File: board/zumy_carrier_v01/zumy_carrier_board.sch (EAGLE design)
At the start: 26 parts, among them IC1 SN74AUP2G17, IC2 SN74AUP2G17, J1 ODROID_POWER, J2 BATT_POWER, SW1 500SSP1S1M6QEA

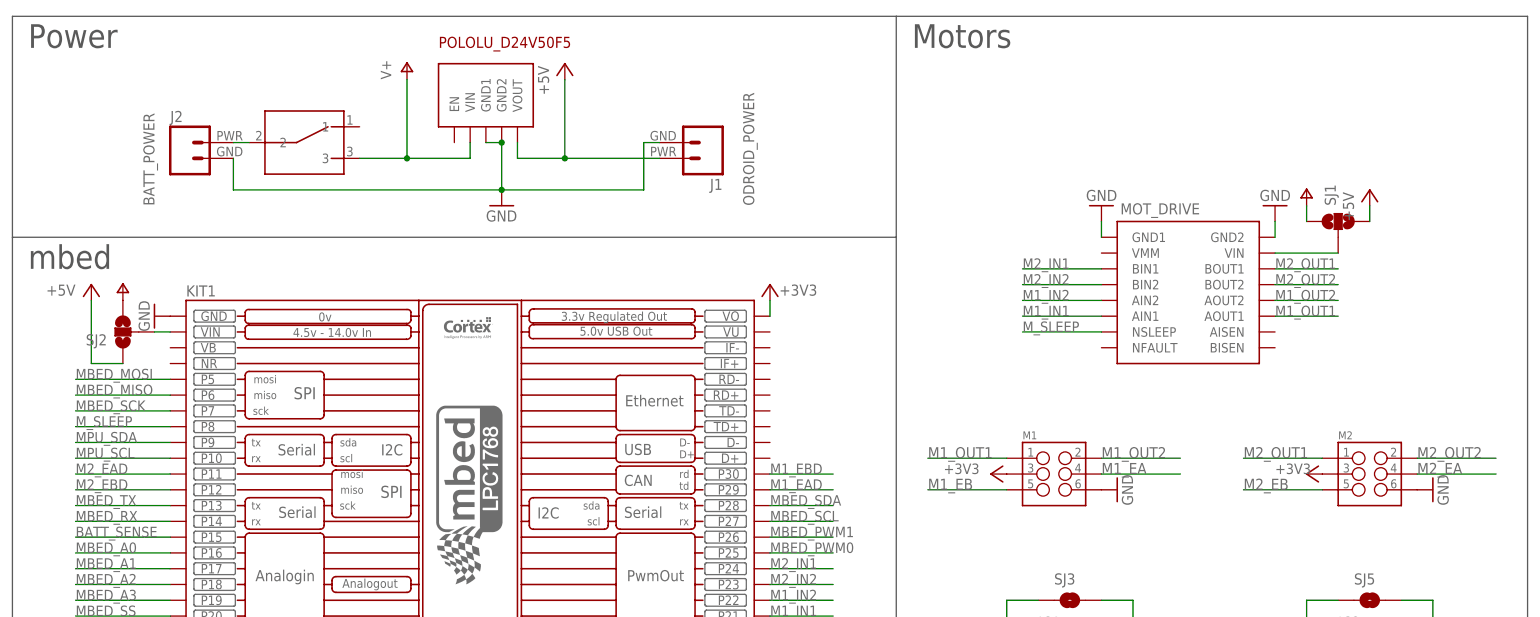
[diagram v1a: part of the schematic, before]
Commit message: Finishing touches for Rev. F. Moved voltage regulator to not conflict with mbed USB cable. Added support post holes for accelerometer and voltage regulator. Increased drill for battery and odroid power. Added hint lines for surface mount components.
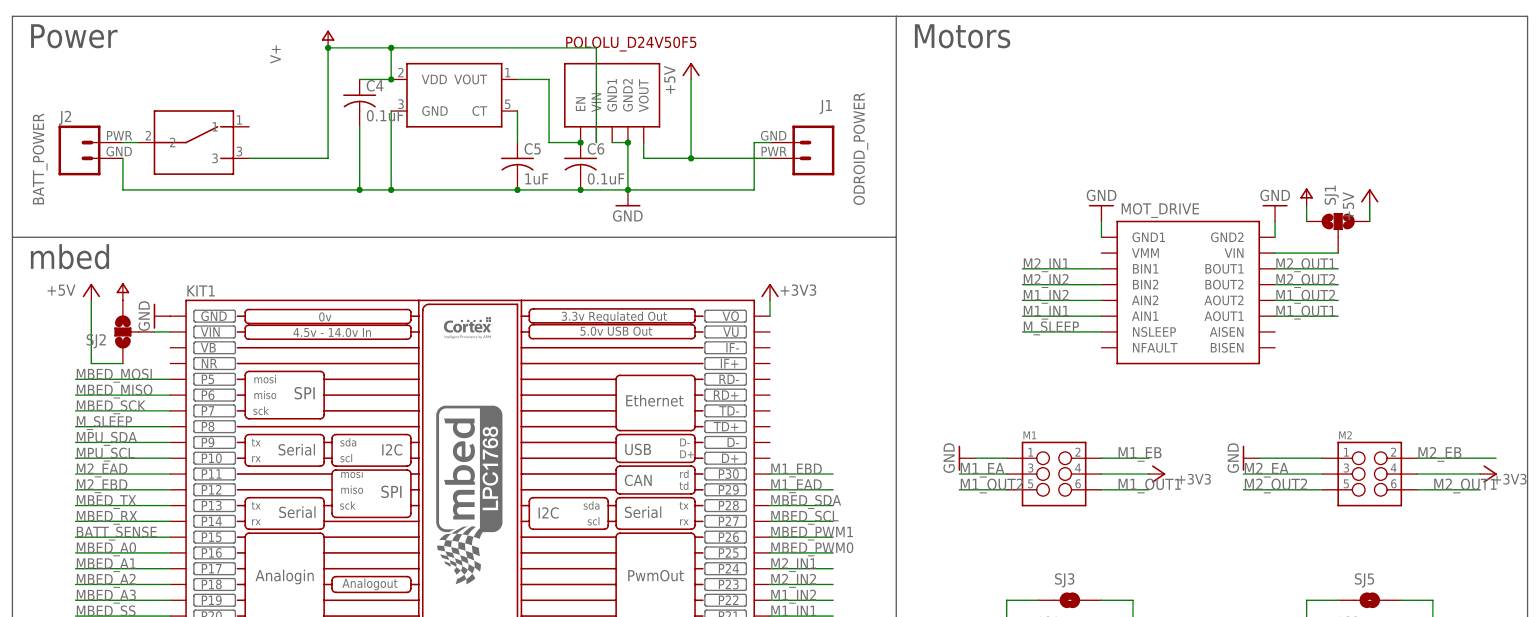
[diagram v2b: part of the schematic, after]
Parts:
- added C4, C6: 0.1uF, rcl:C-USC1206
- added C5: 1uF, rcl:C-USC1206
- added U$2: BD5260G, zumy:BD5260G
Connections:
- new net N$4: C6.1, U$2.VOUT, U$5.EN
- new net N$6: C5.1, U$2.CT
- net +3V3: now also M1.4, M2.4; no longer M1.3, M2.3
- net GND: now also C4.2, C5.2, C6.2, M1.1, M2.1, U$2.GND; no longer M1.6, M2.6
- net M1_EA: now also M1.3; no longer M1.4
- net M1_EB: now also M1.2; no longer M1.5
- net M1_OUT1: now also M1.6; no longer M1.1
- net M1_OUT2: now also M1.5; no longer M1.2
- net M2_EA: now also M2.3; no longer M2.4
- net M2_EB: now also M2.2; no longer M2.5
- net M2_OUT1: now also M2.6; no longer M2.1
- net M2_OUT2: now also M2.5; no longer M2.2
- net V+: now also C4.1, U$2.VDD
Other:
- moved on the sheet: J1, J2

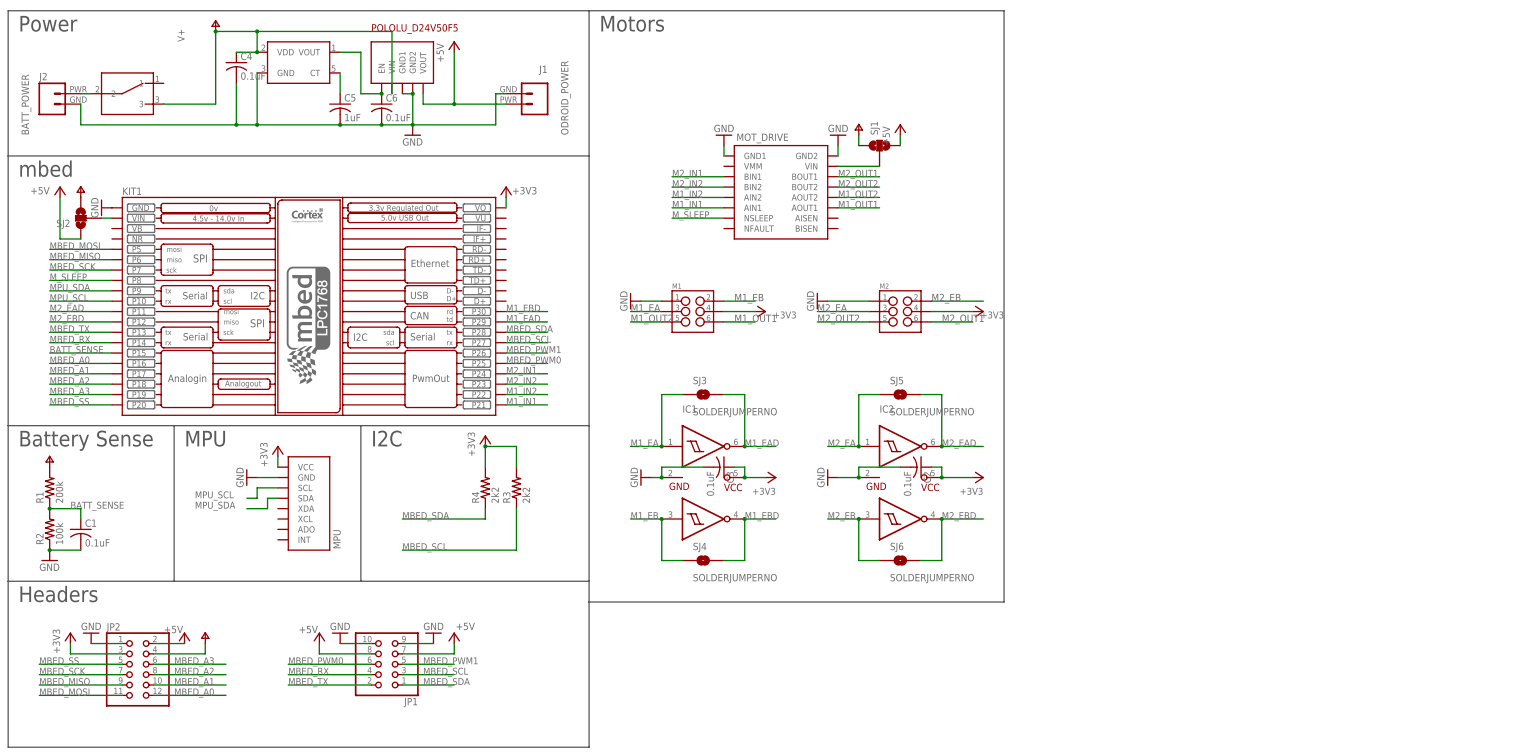
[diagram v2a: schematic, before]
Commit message: Starting to shuffle board around for ODROID-C2 update.
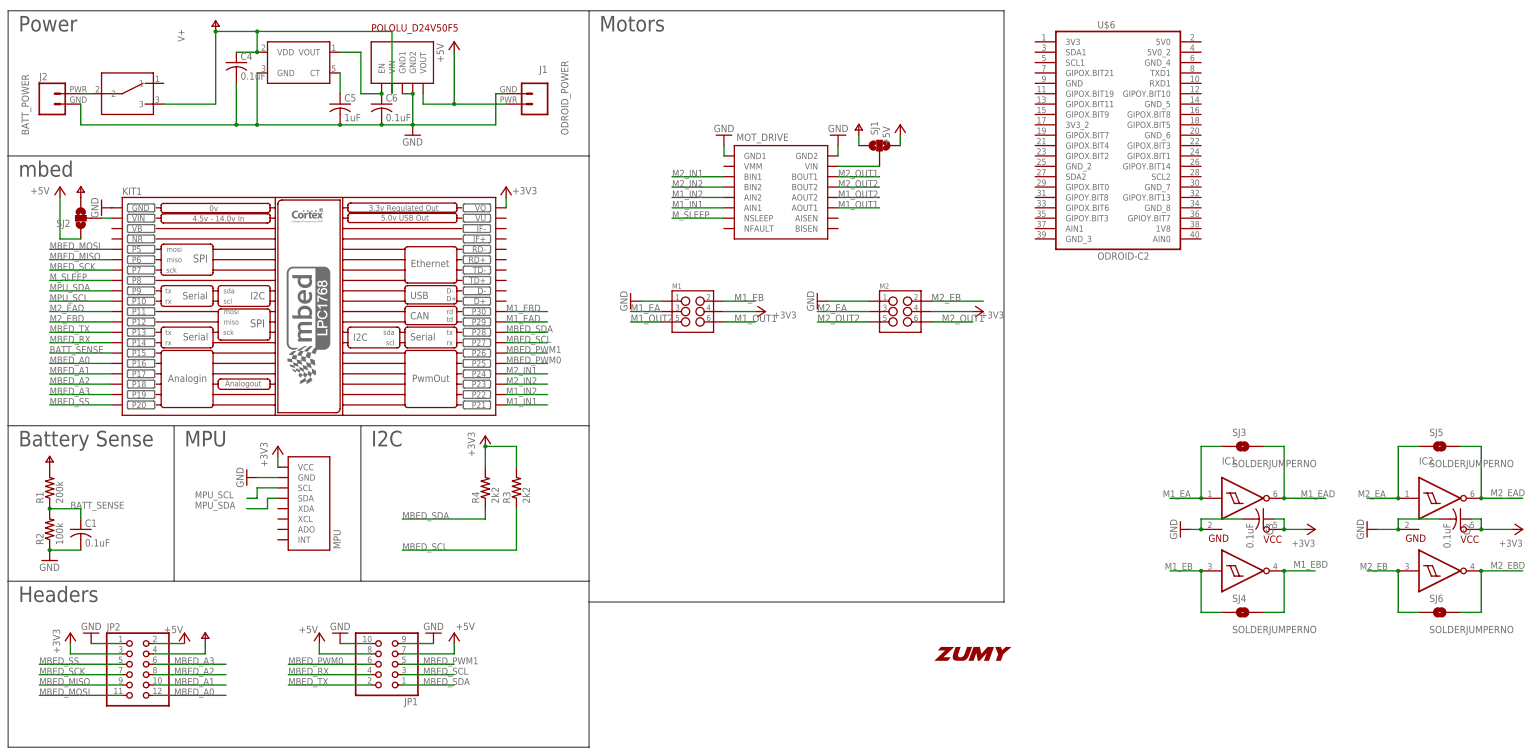
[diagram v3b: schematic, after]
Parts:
- added U$3: ZUMY_LOGO, zumy:ZUMY_LOGO
- added U$6: ODROID-C2, zumy:ODROID-C2
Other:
- moved on the sheet: C2, C3, IC1, IC2, SJ3, SJ4, SJ5, SJ6
